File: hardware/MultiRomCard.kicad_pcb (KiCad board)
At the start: 2 copper layers, 160 x 100 mm, 55 parts, among them P1 VC4000_Cartridge_Bus, P2 MicroSD_Breakout, P3 DISPLAY, P4 JUMPER1, P5 JUMPER2, P6 JUMPER3, P7 JUMPER4, SW1 UP, SW2 DOWN, SW3 SELECT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

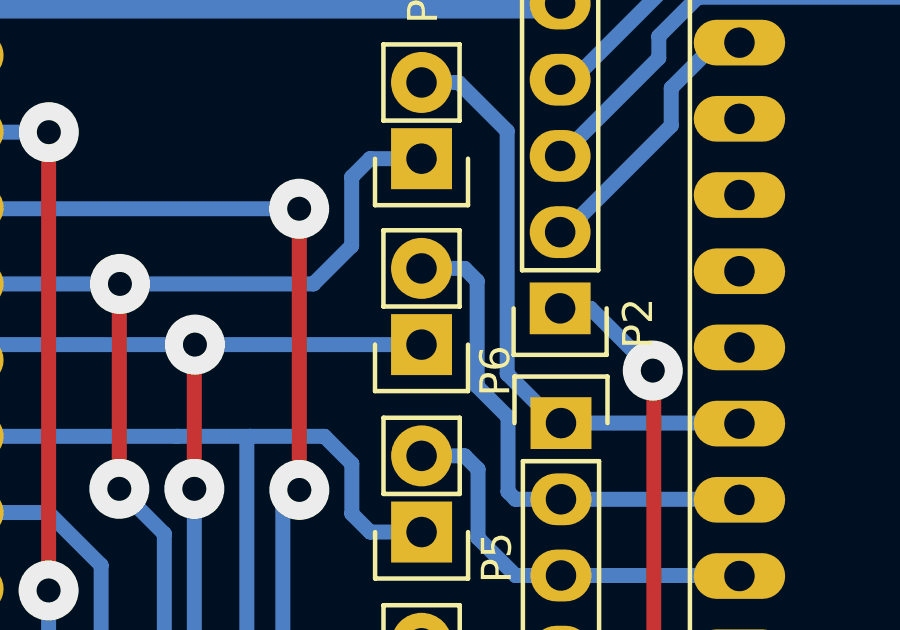
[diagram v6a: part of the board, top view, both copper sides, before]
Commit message: corrected soldermask layer for connector foodprint
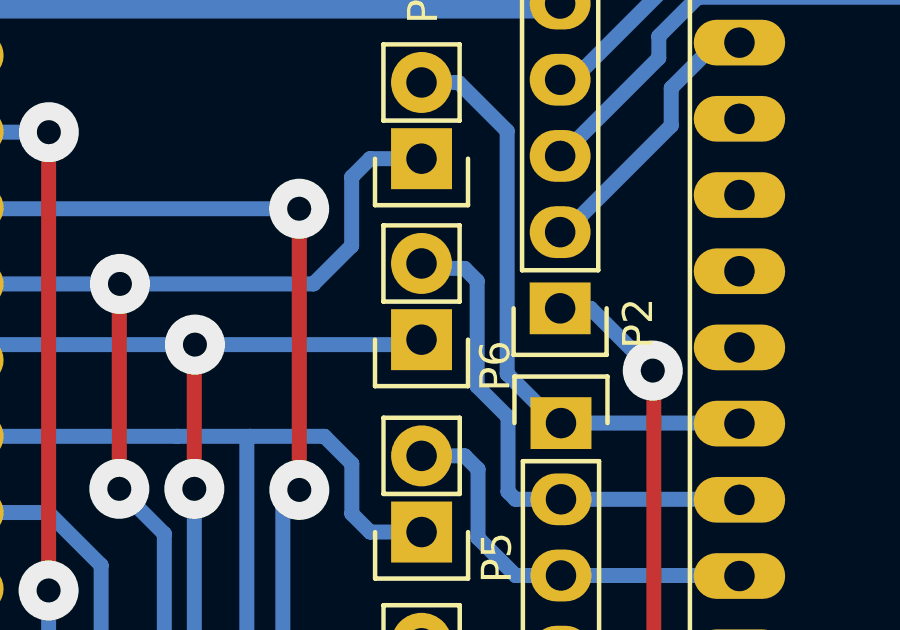
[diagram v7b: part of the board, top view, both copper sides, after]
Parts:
- moved P6 0.17 mm to (103.6, 64.8)
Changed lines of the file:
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@@
-(kicad_pcb (version 4) (host pcbnew 4.0.2-stable)
+(kicad_pcb (version 4) (host pcbnew 4.0.1-stable)
   (general
     (links 228)
@@
     (mod_text_size 1 1)
     (mod_text_width 0.15)
-    (pad_size 1.4 1.4)
-    (pad_drill 0.9)
+    (pad_size 1.524 14)
+    (pad_drill 0)
     (pad_to_mask_clearance 0)
     (aux_axis_origin 0 0)
     (visible_elements FFFFEF7F)
     (pcbplotparams
-      (layerselection 0x00000_80000000)
+      (layerselection 0x010f0_80000001)
       (usegerberextensions false)
-      (excludeedgelayer false)
+      (excludeedgelayer true)
       (linewidth 0.100000)
       (plotframeref false)
@@
       (psnegative false)
       (psa4output false)
-      (plotreference false)
-      (plotvalue false)
+      (plotreference true)
+      (plotvalue true)
       (plotinvisibletext false)
       (padsonsilk false)
       (subtractmaskfromsilk false)
-      (outputformat 4)
+      (outputformat 1)
       (mirror false)
-      (drillshape 2)
+      (drillshape 0)
       (scaleselection 1)
       (outputdirectory Printouts/))
@@
       (effects (font (size 1 1) (thickness 0.15)))
     )
-    (pad 31 connect rect (at 38.1 0 90) (size 1.524 14) (layers B.Cu F.Mask)
+    (pad 31 connect rect (at 38.1 0 90) (size 1.524 14) (layers B.Cu B.Mask)
       (net 1 "Net-(P1-Pad31)"))
-    (pad 30 connect rect (at 35.56 0 90) (size 1.524 14) (layers B.Cu F.Mask)
-      (net 10 VCC))
-    (pad 29 connect rect (at 33.02 0 90) (size 1.524 14) (layers B.Cu F.Mask)
-      (net 20 GND))
-    (pad 28 connect rect (at 30.48 0 90) (size 1.524 14) (layers B.Cu F.Mask)
+    (pad 30 connect rect (at 35.56 0 90) (size 1.524 14) (layers B.Cu B.Mask)
+      (net 10 VCC))
+    (pad 29 connect rect (at 33.02 0 90) (size 1.524 14) (layers B.Cu B.Mask)
+      (net 20 GND))
+    (pad 28 connect rect (at 30.48 0 90) (size 1.524 14) (layers B.Cu B.Mask)
       (net 72 /WRP))
-    (pad 27 connect rect (at 27.94 0 90) (size 1.524 14) (layers B.Cu F.Mask)
+    (pad 27 connect rect (at 27.94 0 90) (size 1.524 14) (layers B.Cu B.Mask)
       (net 73 /RW))
-    (pad 26 connect rect (at 25.4 0 90) (size 1.524 14) (layers B.Cu F.Mask)
+    (pad 26 connect rect (at 25.4 0 90) (size 1.524 14) (layers B.Cu B.Mask)
       (net 74 "Net-(P1-Pad26)"))
-    (pad 25 connect rect (at 22.86 0 90) (size 1.524 14) (layers B.Cu F.Mask)
+    (pad 25 connect rect (at 22.86 0 90) (size 1.524 14) (layers B.Cu B.Mask)
       (net 40 /EA7))
-    (pad 24 connect rect (at 20.32 0 90) (size 1.524 14) (layers B.Cu F.Mask)
+    (pad 24 connect rect (at 20.32 0 90) (size 1.524 14) (layers B.Cu B.Mask)
       (net 41 /EA6))
-    (pad 23 connect rect (at 17.78 0 90) (size 1.524 14) (layers B.Cu F.Mask)
+    (pad 23 connect rect (at 17.78 0 90) (size 1.524 14) (layers B.Cu B.Mask)
       (net 42 /EA5))
-    (pad 22 connect rect (at 15.24 0 90) (size 1.524 14) (layers B.Cu F.Mask)
+    (pad 22 connect rect (at 15.24 0 90) (size 1.524 14) (layers B.Cu B.Mask)
       (net 43 /EA4))
-    (pad 21 connect rect (at 12.7 0 90) (size 1.524 14) (layers B.Cu F.Mask)
+    (pad 21 connect rect (at 12.7 0 90) (size 1.524 14) (layers B.Cu B.Mask)
       (net 44 /EA3))
-    (pad 20 connect rect (at 10.16 0 90) (size 1.524 14) (layers B.Cu F.Mask)
+    (pad 20 connect rect (at 10.16 0 90) (size 1.524 14) (layers B.Cu B.Mask)
       (net 45 /EA2))
-    (pad 19 connect rect (at 7.62 0 90) (size 1.524 14) (layers B.Cu F.Mask)
+    (pad 19 connect rect (at 7.62 0 90) (size 1.524 14) (layers B.Cu B.Mask)
       (net 46 /EA1))
-    (pad 18 connect rect (at 5.08 0 90) (size 1.524 14) (layers B.Cu F.Mask)
+    (pad 18 connect rect (at 5.08 0 90) (size 1.524 14) (layers B.Cu B.Mask)
       (net 47 /EA0))
-    (pad 17 connect rect (at 2.54 0 90) (size 1.524 14) (layers B.Cu F.Mask)
-      (net 10 VCC))
-    (pad 16 connect rect (at 0 0 90) (size 1.524 14) (layers B.Cu F.Mask)
+    (pad 17 connect rect (at 2.54 0 90) (size 1.524 14) (layers B.Cu B.Mask)
+      (net 10 VCC))
+    (pad 16 connect rect (at 0 0 90) (size 1.524 14) (layers B.Cu B.Mask)
       (net 48 /EA8))
-    (pad 15 connect rect (at -2.54 0 90) (size 1.524 14) (layers B.Cu F.Mask)
+    (pad 15 connect rect (at -2.54 0 90) (size 1.524 14) (layers B.Cu B.Mask)
       (net 49 /EA9))
-    (pad 14 connect rect (at -5.08 0 90) (size 1.524 14) (layers B.Cu F.Mask)
+    (pad 14 connect rect (at -5.08 0 90) (size 1.524 14) (layers B.Cu B.Mask)
       (net 71 /EA12))
-    (pad 13 connect rect (at -7.62 0 90) (size 1.524 14) (layers B.Cu F.Mask)
+    (pad 13 connect rect (at -7.62 0 90) (size 1.524 14) (layers B.Cu B.Mask)
       (net 71 /EA12))
-    (pad 12 connect rect (at -10.16 0 90) (size 1.524 14) (layers B.Cu F.Mask)
+    (pad 12 connect rect (at -10.16 0 90) (size 1.524 14) (layers B.Cu B.Mask)
       (net 75 /CE1))
-    (pad 11 connect rect (at -12.7 0 90) (size 1.524 14) (layers B.Cu F.Mask)
+    (pad 11 connect rect (at -12.7 0 90) (size 1.524 14) (layers B.Cu B.Mask)
       (net 50 /EA10))
-    (pad 10 connect rect (at -15.24 0 90) (size 1.524 14) (layers B.Cu F.Mask)
+    (pad 10 connect rect (at -15.24 0 90) (size 1.524 14) (layers B.Cu B.Mask)
       (net 51 /EA11))
-    (pad 9 connect rect (at -17.78 0 90) (size 1.524 14) (layers B.Cu F.Mask)
+    (pad 9 connect rect (at -17.78 0 90) (size 1.524 14) (layers B.Cu B.Mask)
       (net 55 /ED7))
-    (pad 8 connect rect (at -20.32 0 90) (size 1.524 14) (layers B.Cu F.Mask)
+    (pad 8 connect rect (at -20.32 0 90) (size 1.524 14) (layers B.Cu B.Mask)
       (net 56 /ED6))
-    (pad 7 connect rect (at -22.86 0 90) (size 1.524 14) (layers B.Cu F.Mask)
+    (pad 7 connect rect (at -22.86 0 90) (size 1.524 14) (layers B.Cu B.Mask)
       (net 57 /ED5))
-    (pad 6 connect rect (at -25.4 0 90) (size 1.524 14) (layers B.Cu F.Mask)
+    (pad 6 connect rect (at -25.4 0 90) (size 1.524 14) (layers B.Cu B.Mask)
       (net 58 /ED4))
-    (pad 5 connect rect (at -27.94 0 90) (size 1.524 14) (layers B.Cu F.Mask)
+    (pad 5 connect rect (at -27.94 0 90) (size 1.524 14) (layers B.Cu B.Mask)
       (net 59 /ED3))
-    (pad 4 connect rect (at -30.48 0 90) (size 1.524 14) (layers B.Cu F.Mask)
-      (net 20 GND))
-    (pad 3 connect rect (at -33.02 0 90) (size 1.524 14) (layers B.Cu F.Mask)
+    (pad 4 connect rect (at -30.48 0 90) (size 1.524 14) (layers B.Cu B.Mask)
+      (net 20 GND))
+    (pad 3 connect rect (at -33.02 0 90) (size 1.524 14) (layers B.Cu B.Mask)
       (net 52 /ED2))
-    (pad 2 connect rect (at -35.56 0 90) (size 1.524 14) (layers B.Cu F.Mask)
+    (pad 2 connect rect (at -35.56 0 90) (size 1.524 14) (layers B.Cu B.Mask)
       (net 53 /ED1))
-    (pad 1 connect rect (at -38.1 0 90) (size 1.524 14) (layers B.Cu F.Mask)
+    (pad 1 connect rect (at -38.1 0 90) (size 1.524 14) (layers B.Cu B.Mask)
       (net 54 /ED0))
   )
@@
   )
   (module Pin_Headers:Pin_Header_Straight_1x02 (layer F.Cu)
-    (at 103.5653 64.9351 180)
+    (at 103.5653 64.77 180)
     (descr "Through hole pin header")
     (tags "pin header")

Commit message: new pcb version
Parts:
- removed P3: DISPLAY, Pin_Headers:Pin_Header_Straight_1x06
- removed P4: JUMPER1, Pin_Headers:Pin_Header_Straight_1x02
- removed P5: JUMPER2, Pin_Headers:Pin_Header_Straight_1x02
- removed P6: JUMPER3, Pin_Headers:Pin_Header_Straight_1x02
- removed P7: JUMPER4, Pin_Headers:Pin_Header_Straight_1x02
- moved U12 94.3 mm to (114.3, 143.5), turned to 90 degrees
- moved C11 88.7 mm to (109.2, 137.2), turned to 270 degrees
- moved R3 58.3 mm to (111.2, 71.4)
- moved R4 58.3 mm to (108.8, 79.1)
- moved SW2 58.3 mm to (103.3, 70.1)
- moved R2 58.3 mm to (111.2, 87.2)
- moved SW1 58.3 mm to (103.3, 90.5)
- moved SW3 58.3 mm to (103.3, 80.3)
- moved U11 33.2 mm to (119.6, 104.9)
- moved C10 29.4 mm to (114.6, 97.8), turned to 270 degrees
- moved R10 14.3 mm to (132.2, 125.0)
- moved R12 14.3 mm to (132.2, 117.4)
- moved R9 14.3 mm to (132.2, 127.5)
- moved R19 14.3 mm to (105.1, 118.5)
- moved R11 14.3 mm to (132.2, 122.5)
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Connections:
- P1 pad 26: Net-(P1-Pad26) -> (no net)
- P1 pad 31: Net-(P1-Pad31) -> (no net)
- U1 pad 1: Net-(U1-Pad1) -> (no net)
- U1 pad 11: Net-(U1-Pad11) -> (no net)
- U1 pad 12: Net-(U1-Pad12) -> (no net)
- U1 pad 17: Net-(U1-Pad17) -> (no net)
- U1 pad 18: Net-(U1-Pad18) -> (no net)
- U1 pad 19: Net-(U1-Pad19) -> (no net)
- U1 pad 2: Net-(U1-Pad2) -> (no net)
- U1 pad 20: Net-(U1-Pad20) -> (no net)
- U1 pad 21: Net-(P3-Pad1) -> Net-(U1-Pad21)
- U1 pad 22: Net-(P3-Pad2) -> Net-(U1-Pad22)
- U1 pad 23: Net-(P3-Pad3) -> Net-(U1-Pad23)
- U1 pad 24: Net-(P3-Pad4) -> Net-(U1-Pad24)
- U1 pad 25: Net-(U1-Pad25) -> (no net)
- U1 pad 28: Net-(U1-Pad28) -> (no net)
- U1 pad 3: Net-(U1-Pad3) -> (no net)
- U1 pad 30: Net-(U1-Pad30) -> (no net)
- U11 pad 11: Net-(P5-Pad1) -> Net-(U1-Pad23)
- U11 pad 12: Net-(P6-Pad1) -> Net-(U1-Pad22)
- U11 pad 13: Net-(P7-Pad1) -> Net-(U1-Pad21)
- U11 pad 14: Net-(P4-Pad1) -> Net-(U1-Pad24)
- U12 pad 11: Net-(P5-Pad1) -> Net-(U1-Pad23)
- U12 pad 12: Net-(P6-Pad1) -> Net-(U1-Pad22)
- U12 pad 13: Net-(P7-Pad1) -> Net-(U1-Pad21)
- U12 pad 9: Net-(U12-Pad9) -> (no net)
- U3 pad 5: Net-(U3-Pad5) -> (no net)
- U3 pad 6: Net-(U3-Pad6) -> (no net)
- U3 pad 7: Net-(U3-Pad7) -> (no net)
- U4 pad 9: Net-(U4-Pad9) -> (no net)
- U5 pad 1: Net-(U5-Pad1) -> (no net)
- U7 pad 18: Net-(U7-Pad18) -> (no net)
- U7 pad 2: Net-(U7-Pad2) -> (no net)
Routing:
- net VCC: track 609.6 -> 247.5 mm, vias 30 -> 1
- net GND: track 392.3 -> 49.8 mm, vias 22 -> 1
- net OEVCBUS: track 134.2 -> 0.00 mm, vias 6 -> 0
- net Net-(R2-Pad1): track 123.8 -> 0.00 mm, vias 2 -> 0
- net Net-(R16-Pad2): track 119.0 -> 0.00 mm, vias 2 -> 0
- net Net-(R17-Pad2): track 108.8 -> 0.00 mm, vias 2 -> 0
- net CEDBUS: track 86.0 -> 0.35 mm, vias 2 -> 0
- net /A8: track 84.3 -> 0.00 mm, vias 4 -> 0
- net Net-(U1-Pad5): track 83.2 -> 0.00 mm, vias 4 -> 0
- net Net-(R19-Pad2): track 82.8 -> 0.00 mm, vias 2 -> 0
- net Net-(R8-Pad2): track 82.5 -> 0.00 mm
- net Net-(U3-Pad9): track 82.3 -> 0.00 mm, vias 2 -> 0
- net Net-(R18-Pad2): track 81.5 -> 0.00 mm, vias 2 -> 0
- net Net-(U1-Pad6): track 81.5 -> 0.00 mm, vias 2 -> 0
- net Net-(R14-Pad2): track 79.8 -> 0.00 mm
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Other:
- board size 160 x 100 mm -> 137 x 100.1 mm
- net class Default: clearance 0.5 -> 0.254; trace_width 0.5 -> 0.254; via_dia 2 -> 0.8; via_drill 0.8 -> 0.3
- net class Power: clearance 1 -> 0.3; trace_width 1 -> 0.5; via_dia 3 -> 1; via_drill 1 -> 0.5
- rule trace_clearance: 0.5 -> 0.254
- rule via_min_drill: 0.508 -> 0.3
- rule via_min_size: 0.889 -> 0.5
- board text added: "VC4000 MultiROM v0.5 Keller/Maibaum © 2016"
- board text removed: "VC4000 MultiROM v0.4 Keller/Maibaum © 2015/16"
